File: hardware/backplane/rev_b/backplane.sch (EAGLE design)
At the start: 342 parts, among them J0 BACKPLANE_GENERIC_MODULE, J1 BACKPLANE_GENERIC_MODULE, J2 BACKPLANE_GENERIC_MODULE, J3 BACKPLANE_CONTROLLER_MODULE, J4 BACKPLANE_POWER_MODULE, J5 BACKPLANE_GENERIC_MODULE, J6 BACKPLANE_GENERIC_MODULE, J7 BACKPLANE_GENERIC_MODULE, J8 SCREW_TERMINAL, J9 SCREW_TERMINAL, U1 TUSB2077A, U10 SN74LVC2T45, U11 SN74LVC2T45, U12 SN74LVC2T45, U13 SN74LVC2T45, U14 SN74LVC2T45, U15 SN74LVC2T45, U16 SN74LVC2T45, U17 SN74LVC2T45, U18 SN74LVC2T45, U19 SN74LVC2T45, U2 FXMA2102, U20 TS3USB30E, U21 TS3USB30E, U22 TS3USB30E, U23 TS3USB30E, U24 TS3USB30E, U25 TS3USB30E, U26 MCP23008, U27 MCP23008, U28 MCP23008, U29 MCP23008, U3 FXMA2102, U30 MCP23008, U31 MCP23008, U4 FXMA2102, U5 FXMA2102, U6 FXMA2102, U7 FXMA2102, U8 SN74LVC2T45, U9 SN74LVC2T45, Y1 ABMM

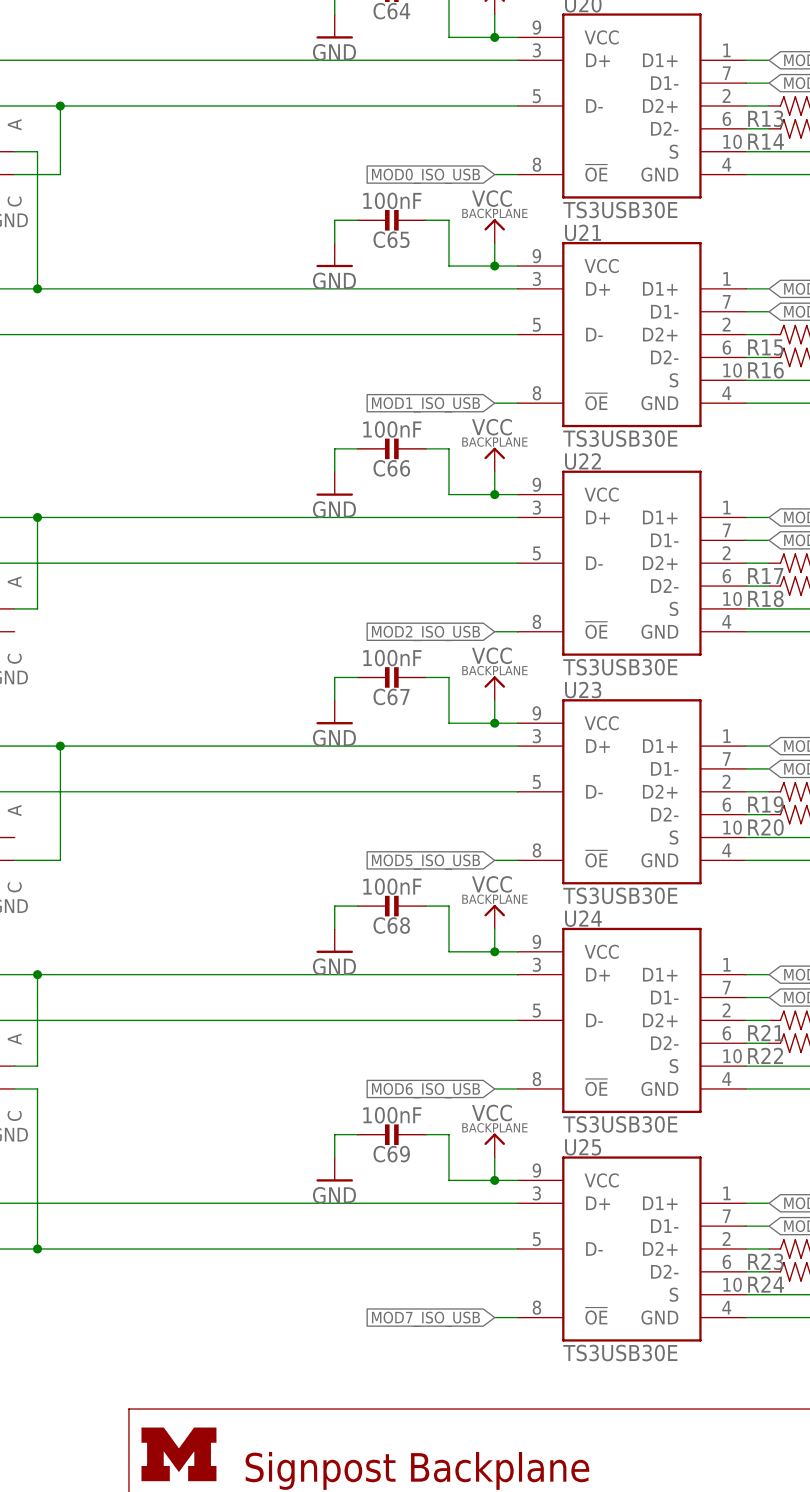
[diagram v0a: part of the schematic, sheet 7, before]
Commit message: backplane: Fix USB data mux control (sch only)
 - Change !OE from MODn_ISO_USB -> MODn_USB_!EN
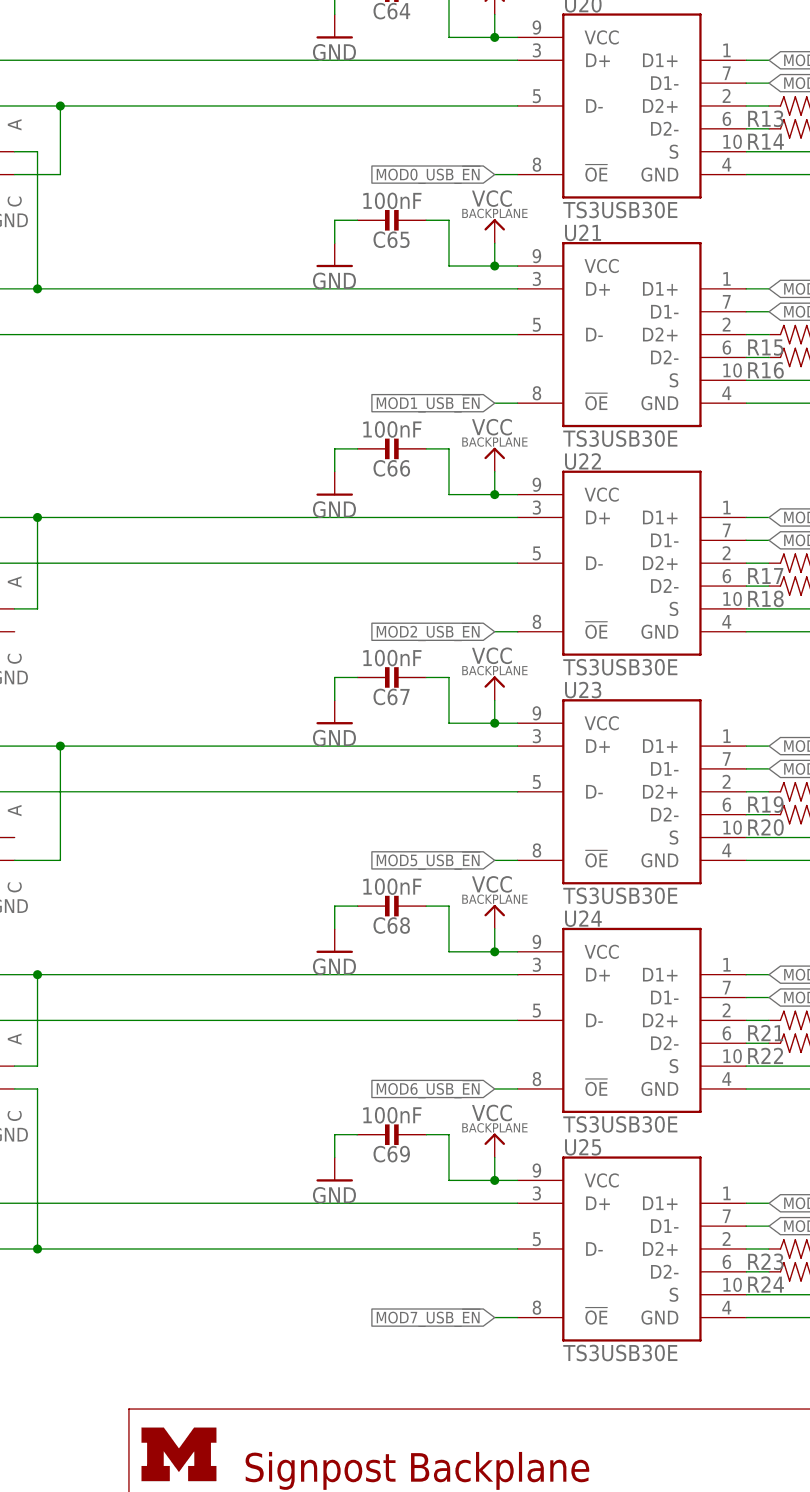
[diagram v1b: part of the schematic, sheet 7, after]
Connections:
- net MOD0_ISO_USB: no longer U20.!OE
- net MOD0_USB_!EN: now also U20.!OE
- net MOD1_ISO_USB: no longer U21.!OE
- net MOD1_USB_!EN: now also U21.!OE
- net MOD2_ISO_USB: no longer U22.!OE
- net MOD2_USB_!EN: now also U22.!OE
- net MOD5_ISO_USB: no longer U23.!OE
- net MOD5_USB_!EN: now also U23.!OE
- net MOD6_ISO_USB: no longer U24.!OE
- net MOD6_USB_!EN: now also U24.!OE
- net MOD7_ISO_USB: no longer U25.!OE
- net MOD7_USB_!EN: now also U25.!OE
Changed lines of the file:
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@@
-</segment>
-</net>
-<net name="MOD0_ISO_USB" class="0">
-<segment>
-<pinref part="U20" gate="G$1" pin="!OE"/>
-<wire x1="187.96" y1="157.48" x2="190.5" y2="157.48" width="0.1524" layer="91"/>
-<label x="187.96" y="157.48" size="1.27" layer="95" rot="R180" xref="yes"/>
-</segment>
-</net>
-<net name="MOD1_ISO_USB" class="0">
-<segment>
-<pinref part="U21" gate="G$1" pin="!OE"/>
-<wire x1="187.96" y1="132.08" x2="190.5" y2="132.08" width="0.1524" layer="91"/>
-<label x="187.96" y="132.08" size="1.27" layer="95" rot="R180" xref="yes"/>
-</segment>
-</net>
-<net name="MOD2_ISO_USB" class="0">
-<segment>
-<pinref part="U22" gate="G$1" pin="!OE"/>
-<wire x1="187.96" y1="106.68" x2="190.5" y2="106.68" width="0.1524" layer="91"/>
-<label x="187.96" y="106.68" size="1.27" layer="95" rot="R180" xref="yes"/>
-</segment>
-</net>
-<net name="MOD5_ISO_USB" class="0">
-<segment>
-<pinref part="U23" gate="G$1" pin="!OE"/>
-<wire x1="187.96" y1="81.28" x2="190.5" y2="81.28" width="0.1524" layer="91"/>
-<label x="187.96" y="81.28" size="1.27" layer="95" rot="R180" xref="yes"/>
-</segment>
-</net>
-<net name="MOD6_ISO_USB" class="0">
-<segment>
-<pinref part="U24" gate="G$1" pin="!OE"/>
-<wire x1="187.96" y1="55.88" x2="190.5" y2="55.88" width="0.1524" layer="91"/>
-<label x="187.96" y="55.88" size="1.27" layer="95" rot="R180" xref="yes"/>
-</segment>
-</net>
-<net name="MOD7_ISO_USB" class="0">
-<segment>
-<pinref part="U25" gate="G$1" pin="!OE"/>
-<wire x1="187.96" y1="30.48" x2="190.5" y2="30.48" width="0.1524" layer="91"/>
-<label x="187.96" y="30.48" size="1.27" layer="95" rot="R180" xref="yes"/>
 </segment>
 </net>
@@
 </segment>
 </net>
+<net name="MOD7_USB_!EN" class="0">
+<segment>
+<pinref part="U25" gate="G$1" pin="!OE"/>
+<wire x1="187.96" y1="30.48" x2="190.5" y2="30.48" width="0.1524" layer="91"/>
+<label x="187.96" y="30.48" size="1.27" layer="95" rot="R180" xref="yes"/>
+</segment>
+</net>
+<net name="MOD6_USB_!EN" class="0">
+<segment>
+<pinref part="U24" gate="G$1" pin="!OE"/>
+<wire x1="187.96" y1="55.88" x2="190.5" y2="55.88" width="0.1524" layer="91"/>
+<label x="187.96" y="55.88" size="1.27" layer="95" rot="R180" xref="yes"/>
+</segment>
+</net>
+<net name="MOD5_USB_!EN" class="0">
+<segment>
+<pinref part="U23" gate="G$1" pin="!OE"/>
+<wire x1="187.96" y1="81.28" x2="190.5" y2="81.28" width="0.1524" layer="91"/>
+<label x="187.96" y="81.28" size="1.27" layer="95" rot="R180" xref="yes"/>
+</segment>
+</net>
+<net name="MOD2_USB_!EN" class="0">
+<segment>
+<pinref part="U22" gate="G$1" pin="!OE"/>
+<wire x1="187.96" y1="106.68" x2="190.5" y2="106.68" width="0.1524" layer="91"/>
+<label x="187.96" y="106.68" size="1.27" layer="95" rot="R180" xref="yes"/>
+</segment>
+</net>
+<net name="MOD1_USB_!EN" class="0">
+<segment>
+<pinref part="U21" gate="G$1" pin="!OE"/>
+<wire x1="187.96" y1="132.08" x2="190.5" y2="132.08" width="0.1524" layer="91"/>
+<label x="187.96" y="132.08" size="1.27" layer="95" rot="R180" xref="yes"/>
+</segment>
+</net>
+<net name="MOD0_USB_!EN" class="0">
+<segment>
+<pinref part="U20" gate="G$1" pin="!OE"/>
+<wire x1="187.96" y1="157.48" x2="190.5" y2="157.48" width="0.1524" layer="91"/>
+<label x="187.96" y="157.48" size="1.27" layer="95" rot="R180" xref="yes"/>
+</segment>
+</net>

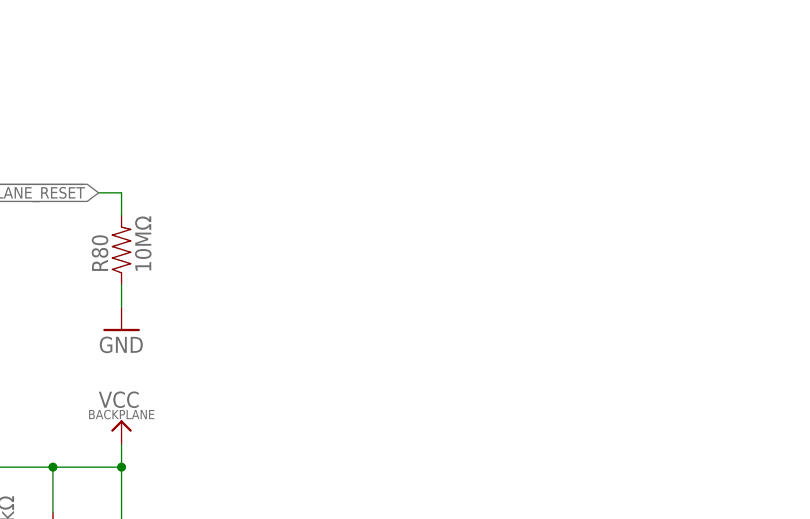
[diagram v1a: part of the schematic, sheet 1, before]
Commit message: backplane: add jumper for !BACKPLANE_RESET
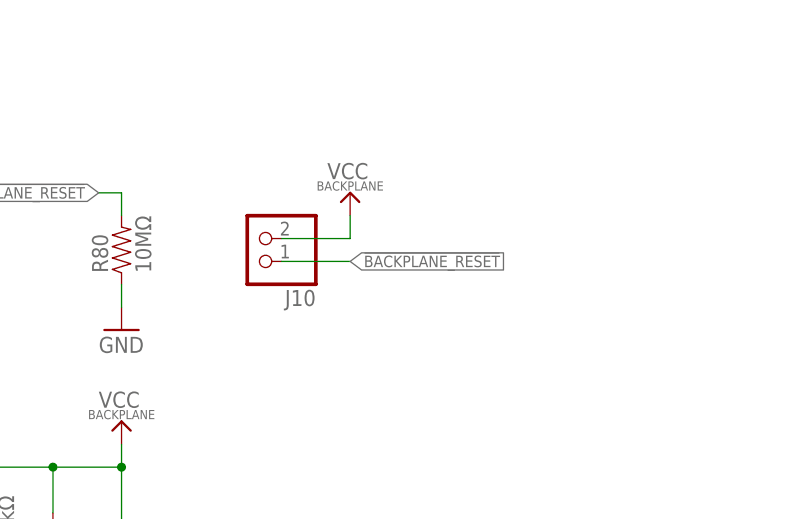
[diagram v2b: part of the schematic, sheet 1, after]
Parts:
- added J10: (no value), pinhead:PINHD-1X2
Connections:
- net !BACKPLANE_RESET: now also J10.1
- net VCC_BACKPLANE: now also J10.2
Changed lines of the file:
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@@
 <part name="TP31" library="headers" deviceset="TEST_POINT_0.040IN" device=""/>
 <part name="TP10" library="headers" deviceset="TEST_POINT_0.040IN" device=""/>
+<part name="J10" library="pinhead" deviceset="PINHD-1X2" device=""/>
+<part name="U$51" library="signpost" deviceset="VCC_BACKPLANE" device=""/>
 </parts>
 <sheets>
@@
 <instance part="J9" gate="G$1" x="190.5" y="50.8" rot="R180"/>
 <instance part="LOGO1" gate="G$1" x="2.54" y="172.72"/>
+<instance part="J10" gate="G$1" x="177.8" y="160.02" rot="R180"/>
+<instance part="U$51" gate="G$1" x="187.96" y="162.56"/>
 </instances>
 <busses>
@@
 <junction x="162.56" y="104.14"/>
 </segment>
+<segment>
+<pinref part="J10" gate="G$1" pin="2"/>
+<pinref part="U$51" gate="G$1" pin="VCC_BACKPLANE"/>
+<wire x1="180.34" y1="160.02" x2="187.96" y2="160.02" width="0.1524" layer="91"/>
+<wire x1="187.96" y1="160.02" x2="187.96" y2="162.56" width="0.1524" layer="91"/>
+</segment>
 </net>
 <net name="MOD0_5V_METERED" class="0">
@@
 <label x="160.02" y="165.1" size="1.27" layer="95" rot="R180" xref="yes"/>
 </segment>
-</net>
+<segment>
+<pinref part="J10" gate="G$1" pin="1"/>
+<wire x1="187.96" y1="157.48" x2="180.34" y2="157.48" width="0.1524" layer="91"/>
+<label x="187.96" y="157.48" size="1.27" layer="95" xref="yes"/>
+</segment>
+</net>

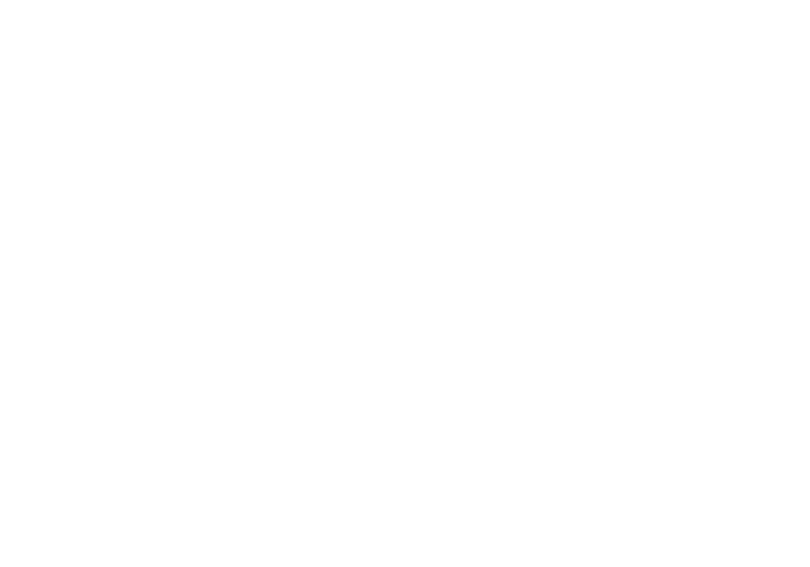
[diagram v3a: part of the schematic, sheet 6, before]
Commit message: backplane: add pull-downs to unusued hub port
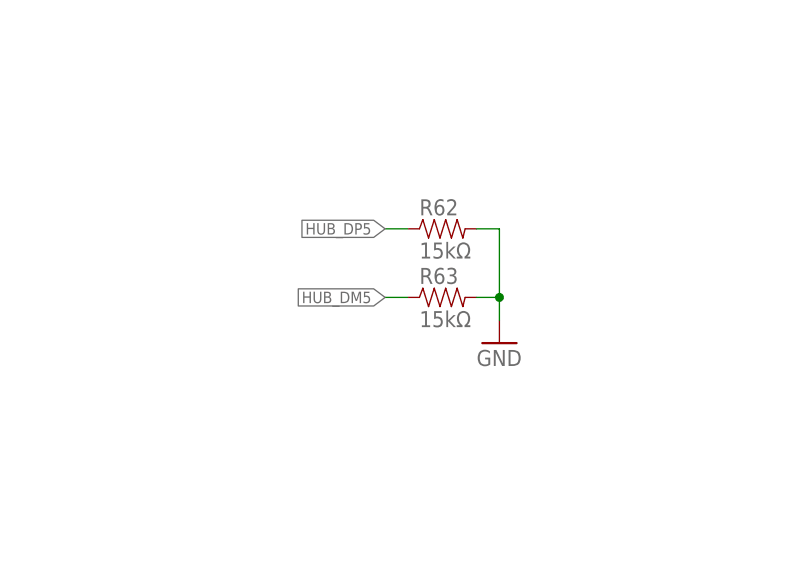
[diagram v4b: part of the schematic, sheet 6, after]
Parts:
- added R81, R82: 10MΩ, passives:RESISTOR0603_RES
- R62, R63: value 10MΩ -> 15kΩ
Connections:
- net !BACKPLANE_RESET: now also R82.2; no longer R80.2
- net GND: now also R62.2, R63.2, R81.1, R82.1; no longer R62.1, R63.1
- net HUB_DM5: now also R63.1
- net HUB_DP5: now also R62.1
- net MOD0_ISO_I2C: now also R65.2; no longer R63.2
- net MOD0_ISO_POWER: now also R64.2; no longer R62.2
- net MOD0_ISO_USB: now also R66.2; no longer R64.2
- net MOD1_ISO_I2C: now also R68.2; no longer R66.2
- net MOD1_ISO_POWER: now also R67.2; no longer R65.2
- net MOD1_ISO_USB: now also R69.2; no longer R67.2
- net MOD2_ISO_I2C: now also R71.2; no longer R69.2
- net MOD2_ISO_POWER: now also R70.2; no longer R68.2
- net MOD2_ISO_USB: now also R72.2; no longer R70.2
- net MOD5_ISO_I2C: now also R74.2; no longer R72.2
- net MOD5_ISO_POWER: now also R73.2; no longer R71.2
- net MOD5_ISO_USB: now also R75.2; no longer R73.2
- net MOD6_ISO_I2C: now also R77.2; no longer R75.2
- net MOD6_ISO_POWER: now also R76.2; no longer R74.2
- net MOD6_ISO_USB: now also R78.2; no longer R76.2
- net MOD7_ISO_I2C: now also R80.2; no longer R78.2
- net MOD7_ISO_POWER: now also R79.2; no longer R77.2
- net MOD7_ISO_USB: now also R81.2; no longer R79.2
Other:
- note added: "Tie unused ports to GND"
- note added: "https://e2e.ti.com/support/interface/digital_interface/f/130/p/367935/1295211#1295211"
- moved on the sheet: R64, R65, R66, R67, R68, R69, R70, R71, R72, R73, R74, R75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

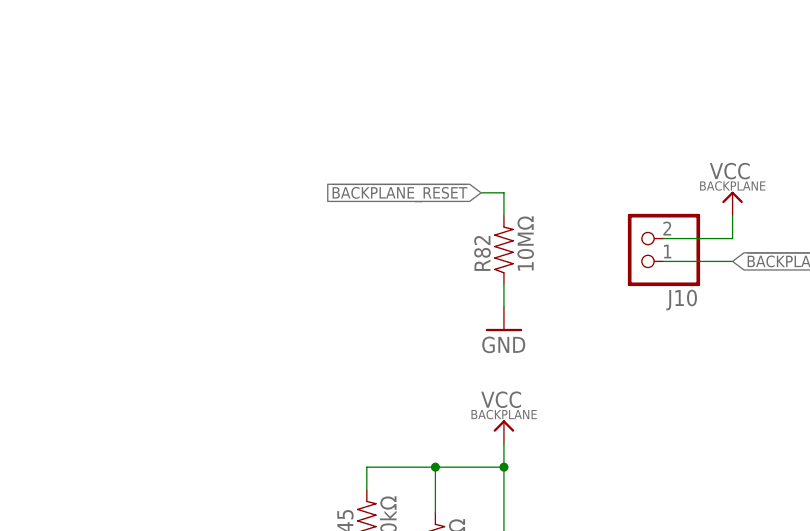
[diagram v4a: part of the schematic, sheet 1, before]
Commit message: Change `!BACKPLANE_RESET` to pull up by default
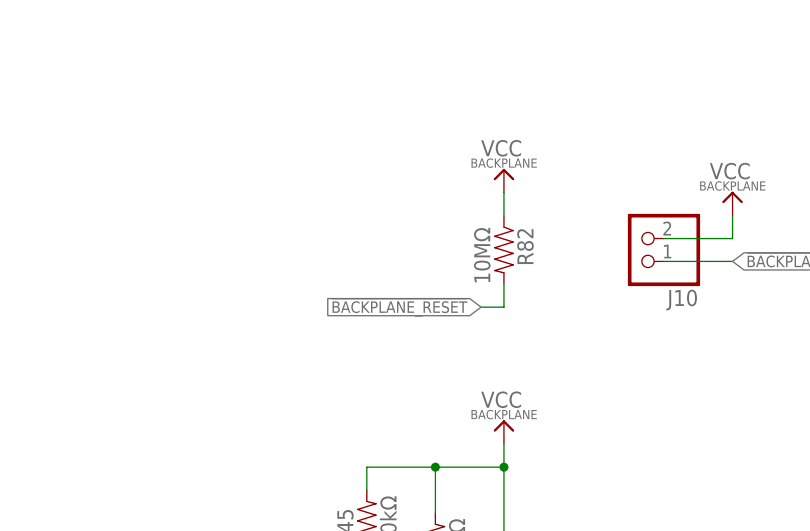
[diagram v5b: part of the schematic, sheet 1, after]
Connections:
- net GND: no longer R82.1
- net VCC_BACKPLANE: now also R82.1
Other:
- moved on the sheet: R82
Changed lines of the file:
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@@
 <part name="U$42" library="signpost" deviceset="VCC_BACKPLANE" device=""/>
 <part name="R82" library="passives" deviceset="RESISTOR" device="0603_RES" value="10MΩ"/>
-<part name="GND72" library="umich" deviceset="GND" device=""/>
 <part name="R45" library="passives" deviceset="RESISTOR" device="0603_RES" value="10kΩ"/>
 <part name="R46" library="passives" deviceset="RESISTOR" device="0603_RES" value="10kΩ"/>
@@
 <part name="R63" library="passives" deviceset="RESISTOR" device="0603_RES" value="15kΩ"/>
 <part name="GND142" library="umich" deviceset="GND" device=""/>
+<part name="U$52" library="signpost" deviceset="VCC_BACKPLANE" device=""/>
 </parts>
 <sheets>
@@
 <instance part="U$41" gate="G$1" x="93.98" y="73.66"/>
 <instance part="U$42" gate="G$1" x="101.6" y="73.66"/>
-<instance part="R82" gate="G$1" x="162.56" y="160.02" rot="R90"/>
-<instance part="GND72" gate="1" x="162.56" y="149.86"/>
+<instance part="R82" gate="G$1" x="162.56" y="157.48" rot="R270"/>
 <instance part="R45" gate="G$1" x="147.32" y="129.54" rot="R90"/>
 <instance part="R46" gate="G$1" x="154.94" y="127" rot="R90"/>
@@
 <instance part="J10" gate="G$1" x="177.8" y="160.02" rot="R180"/>
 <instance part="U$51" gate="G$1" x="187.96" y="162.56"/>
+<instance part="U$52" gate="G$1" x="162.56" y="165.1"/>
 </instances>
 <busses>
@@
 <wire x1="68.58" y1="99.06" x2="88.9" y2="99.06" width="0.1524" layer="91"/>
 <wire x1="88.9" y1="99.06" x2="88.9" y2="93.98" width="0.1524" layer="91"/>
-</segment>
-<segment>
-<pinref part="GND72" gate="1" pin="GND"/>
-<pinref part="R82" gate="G$1" pin="1"/>
-<wire x1="162.56" y1="152.4" x2="162.56" y2="154.94" width="0.1524" layer="91"/>
 </segment>
 </net>
@@
 <wire x1="187.96" y1="160.02" x2="187.96" y2="162.56" width="0.1524" layer="91"/>
 </segment>
+<segment>
+<pinref part="R82" gate="G$1" pin="1"/>
+<pinref part="U$52" gate="G$1" pin="VCC_BACKPLANE"/>
+<wire x1="162.56" y1="162.56" x2="162.56" y2="165.1" width="0.1524" layer="91"/>
+</segment>
 </net>
 <net name="MOD0_5V_METERED" class="0">
@@
 <segment>
 <pinref part="R82" gate="G$1" pin="2"/>
-<wire x1="162.56" y1="162.56" x2="162.56" y2="165.1" width="0.1524" layer="91"/>
-<wire x1="162.56" y1="165.1" x2="160.02" y2="165.1" width="0.1524" layer="91"/>
-<label x="160.02" y="165.1" size="1.27" layer="95" rot="R180" xref="yes"/>
-</segment>
-<segment>
+<wire x1="162.56" y1="154.94" x2="162.56" y2="152.4" width="0.1524" layer="91"/>
+<wire x1="162.56" y1="152.4" x2="160.02" y2="152.4" width="0.1524" layer="91"/>
+<label x="160.02" y="152.4" size="1.27" layer="95" rot="R180" xref="yes"/>
+</segment>
+<segment>
